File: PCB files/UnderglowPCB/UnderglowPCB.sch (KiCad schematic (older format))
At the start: 67 parts, among them J1 USB_B_Micro, J12 DB9_Male, J4 Conn_01x07, J5 Conn_01x05, J7 Screw_Terminal_01x03, J8 Screw_Terminal_01x03, Q1 S8050, Q2 S8050, SW1 SW_Push, U1 CP2102N-A01-GQFN28, U2 TPS62133, U3 74HC14, U4 74HC14, U5 LD56100DPU33R, U6 ESP32-WROOM-32D, U7 SN65HVD230, U8 USBLC6-2SC6

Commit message: Version 1.0.0 of PCB is almost done. Need tooling holes and holds for DB9 mount.
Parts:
- removed SW1: SW_Push, Button_Switch_SMD:SW_SPST_TL3305A, symbol Switch:SW_Push
- J1: footprint Connector_USB:USB_Micro-B_Molex-105017-0001 -> Connector_USB:USB_Micro-AB_Molex_47590-0001
- J10, J11, J3, J6, J9: renamed from J?; footprint TerminalBlock_Phoenix:TerminalBlock_Phoenix_MKDS-1,5-3-5.08_1x03_P5.08mm_Horizontal -> Connector_PinHeader_2.54mm:PinHeader_1x03_P2.54mm_Vertical
- J2: renamed from J?; footprint TerminalBlock_Phoenix:TerminalBlock_Phoenix_MKDS-1,5-3-5.08_1x03_P5.08mm_Horizontal -> Connector_PinSocket_2.54mm:PinSocket_1x03_P2.54mm_Vertical
- J7, J8: footprint TerminalBlock_Phoenix:TerminalBlock_Phoenix_MKDS-1,5-3-5.08_1x03_P5.08mm_Horizontal -> Connector_PinHeader_2.54mm:PinHeader_1x03_P2.54mm_Vertical
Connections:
- net labels added: CAR_12V
- wire segments 167 -> 162
- no-connect marks 33 -> 31
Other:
- moved on the sheet: D4

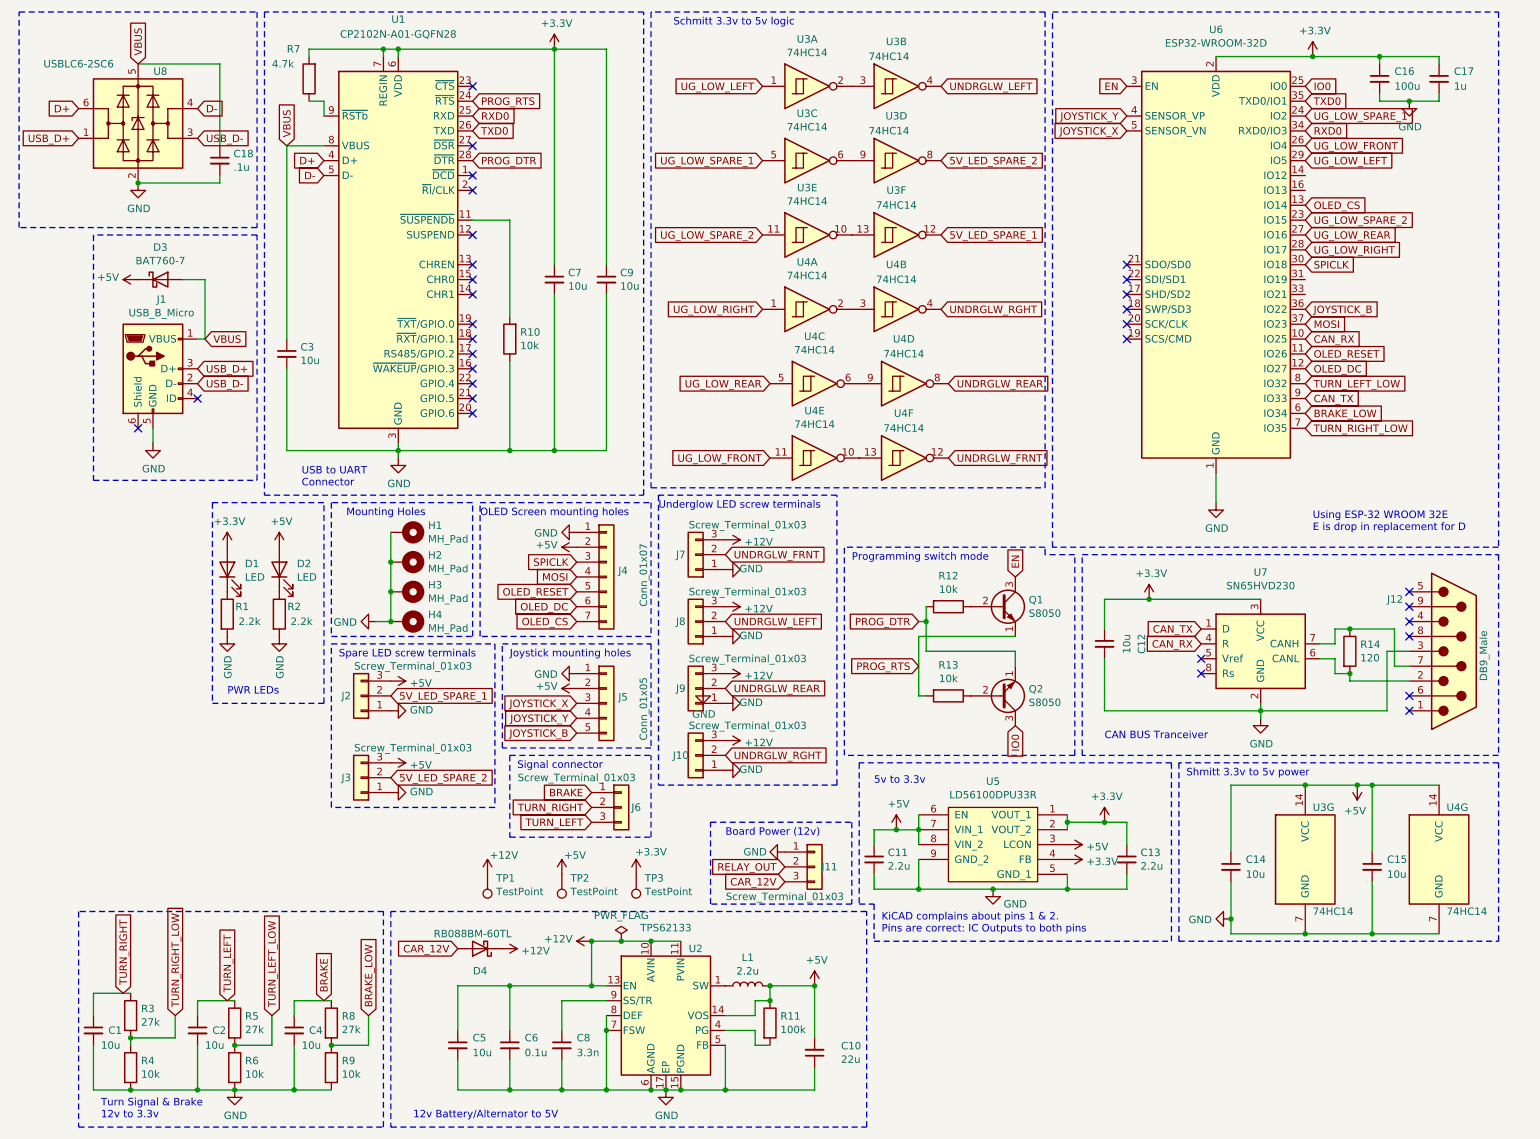
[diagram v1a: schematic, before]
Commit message: Posted to reddit, changes include TVS Zener diodes and new power solution. That's a lot bigger.
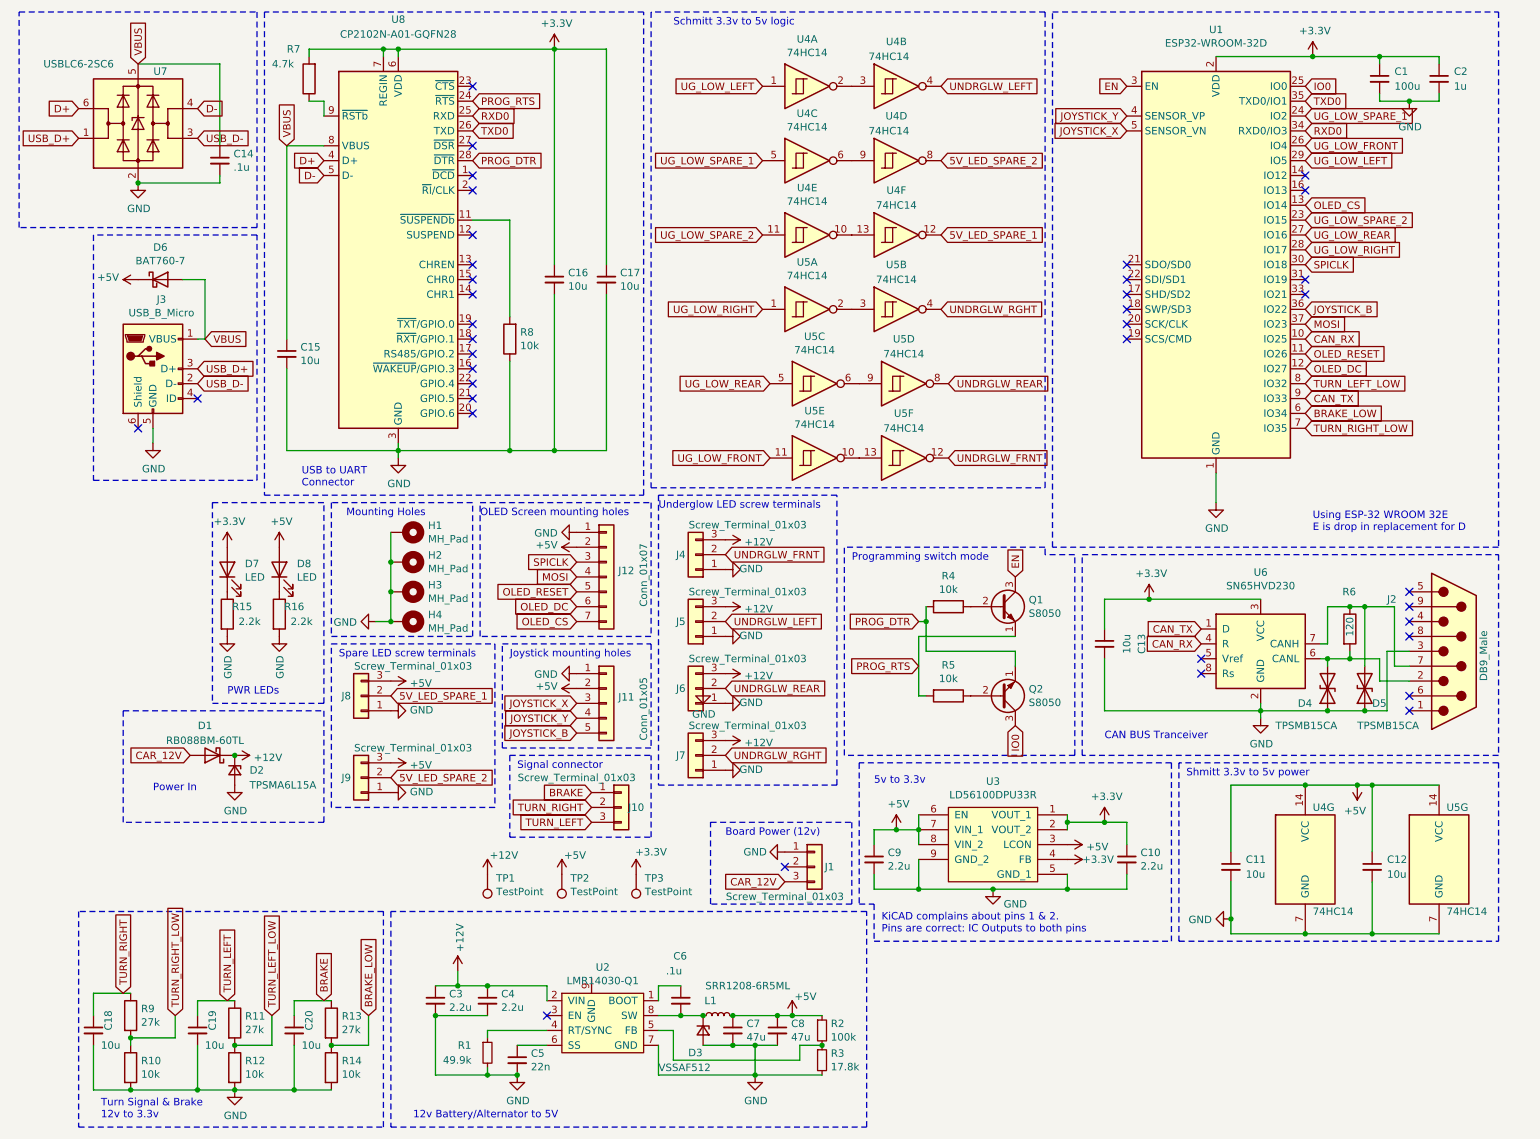
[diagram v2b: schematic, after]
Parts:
- removed C10: 22u, Capacitor_SMD:C_0805_2012Metric, symbol Device:C_Small
- removed L1: 2.2u, Inductor_SMD:L_Coilcraft_XxL4020, symbol Device:L
- removed R11: 100k, Resistor_SMD:R_0603_1608Metric, symbol Device:R
- removed U2: TPS62133, Package_DFN_QFN:VQFN-16-1EP_3x3mm_P0.5mm_EP1.68x1.68mm_ThermalVias, symbol Regulator_Switching:TPS62133
- added C3, C4: 2.2u, Capacitor_SMD:C_0603_1608Metric, symbol Device:C_Small
- added C7: 47u, Capacitor_SMD:C_1210_3225Metric, symbol Device:C_Small
- added D2: TPSMA6L15A, UnderglowPCB:TPSMA6L15A, symbol Device:D_Zener_Small
- added D3: VSSAF512, UnderglowPCB:TPSMA6L15A, symbol Device:D_Zener_Small
- added D4, D5: TPSMB15CA, UnderglowPCB:TPSMB15CA, symbol Device:D_TVS
- added L1: SRR1208-6R5ML, UnderglowPCB:SRR1208, symbol Device:L_Small
- added R1: 49.9k, Resistor_SMD:R_0603_1608Metric, symbol Device:R_Small
- added R2: 100k, Resistor_SMD:R_0603_1608Metric, symbol Device:R_Small
- added R3: 17.8k, Resistor_SMD:R_0603_1608Metric, symbol Device:R_Small
- added U2: LMR14030-Q1, Package_SO:Texas_HSOP-8-1EP_3.9x4.9mm_P1.27mm_ThermalVias, symbol ExternalPartsLib:LMR14030-Q1
- C14: renamed from C18; footprint Capacitor_SMD:C_0402_1005Metric -> Capacitor_SMD:C_0603_1608Metric
- C5: value 10u -> 22n; footprint Capacitor_SMD:C_1210_3225Metric -> Capacitor_SMD:C_0603_1608Metric
- C6: value 0.1u -> .1u
- C8: value 3.3n -> 47u; footprint Capacitor_SMD:C_0603_1608Metric -> Capacitor_SMD:C_1210_3225Metric
- renumbered C16 to C1, C13 to C10, C14 to C11, C15 to C12, C12 to C13, C3 to C15, C7 to C16, C9 to C17, C1 to C18, C2 to C19, C17 to C2, C4 to C20, C11 to C9, D4 to D1, D3 to D6, D1 to D7, D2 to D8, J11 to J1, J6 to J10, J5 to J11, J4 to J12, J12 to J2, J1 to J3, J7 to J4, J8 to J5, J9 to J6, J10 to J7, J2 to J8, J3 to J9, R4 to R10, R5 to R11, R6 to R12, R8 to R13, R9 to R14, R1 to R15, R2 to R16, R12 to R4, R13 to R5, R14 to R6, R10 to R8, R3 to R9, U6 to U1, U5 to U3, U3 to U4, U4 to U5, U7 to U6, U8 to U7, U1 to U8
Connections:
- net +12V: now also C3.1, C4.1, D2.1 (K), U2.2 (VIN); no longer C5.1, C6.1
- net +5V: now also C8.1, C7.1, L1.2, R2.1
- net GND: now also C3.2, C4.2, C7.2, D2.2 (A), D3.2 (A), D4.1 (A1), D5.1 (A1), R1.2, R3.2, U2.7 (GND); no longer C6.2
- net at J2.2, R6.2, U6.6 (CANL): now also D4.2 (A2)
- net at J2.7, R6.1, U6.7 (CANH): now also D5.2 (A2)
- net RELAY_OUT: no longer names the net of J1.2 (Pin_2)
- new net: C6.1, U2.1 (BOOT)
- new net: R1.1, U2.4 (RT/SYNC)
- new net: R2.2, R3.1, U2.5 (FB)
- new net: C5.1, U2.6 (SS)
- new net: C6.2, D3.1 (K), L1.1, U2.8 (SW)
- no-connect marks 31 -> 37
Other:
- note added: "Power In"
- moved on the sheet: D1, R6

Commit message: Lastest draft of device
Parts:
- removed TP1, TP2, TP3: TestPoint, TestPoint:TestPoint_Plated_Hole_D2.0mm, symbol Connector:TestPoint
- removed U3: LD56100DPU33R, UnderglowPCB:LD56100DPU33R, symbol ExternalPartsLib:LD56100DPU33R
- added F1: 3413.0330.22, Fuse:Fuse_1206_3216Metric, symbol Device:Fuse_Small
- added U3: NCP1117-3.3_SOT223, Package_TO_SOT_SMD:SOT-223-3_TabPin2, symbol Regulator_Linear:NCP1117-3.3_SOT223
- C10, C9: value 2.2u -> 10u
- J2: footprint Connector_Dsub:DSUB-9_Male_Horizontal_P2.77x2.84mm_EdgePinOffset9.40mm -> UnderglowPCB:DB9
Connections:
- net +12V: no longer D2.1 (K)
- net +3V3: now also J11.2 (Pin_2), U3.2 (VO)
- net +5V: now also U3.3 (VI); no longer J11.2 (Pin_2)
- net 5V_LED_SPARE_1: now also U4.10; no longer U4.12
- net 5V_LED_SPARE_2: now also U4.8; no longer U4.8
- net CAR_12V: now also D2.1 (K), F1.1; no longer D1.2 (A)
- net GND: now also U2.9 (GND), U3.1 (GND)
- net UG_LOW_FRONT: now also U5.1; no longer U5.11
- net UG_LOW_LEFT: now also U5.3; no longer U4.1
- net UG_LOW_REAR: now also U5.5; no longer U5.5
- net UG_LOW_RIGHT: now also U4.1; no longer U5.1
- net UG_LOW_SPARE_1: now also U4.5; no longer U4.5
- net UG_LOW_SPARE_2: now also U4.3; no longer U4.11
- net UNDRGLW_FRNT: now also U5.12; no longer U5.12
- net UNDRGLW_LEFT: now also U5.10; no longer U4.4
- net UNDRGLW_REAR: now also U5.8; no longer U5.8
- net UNDRGLW_RGHT: now also U4.12; no longer U5.4
- net at U4.2: now also U4.13; no longer U4.3
- net at U5.2: now also U5.13; no longer U5.3
- new net: D1.2 (A), F1.2
- new net: U4.11, U4.4
- new net: U4.6, U4.9
- new net: U5.11, U5.4
- new net: U5.6, U5.9
- no-connect marks 37 -> 40
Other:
- note removed: "KiCAD complains about pins 1 & 2.\nPins are correct: IC Outputs to both pins"
- moved on the sheet: D1, D2

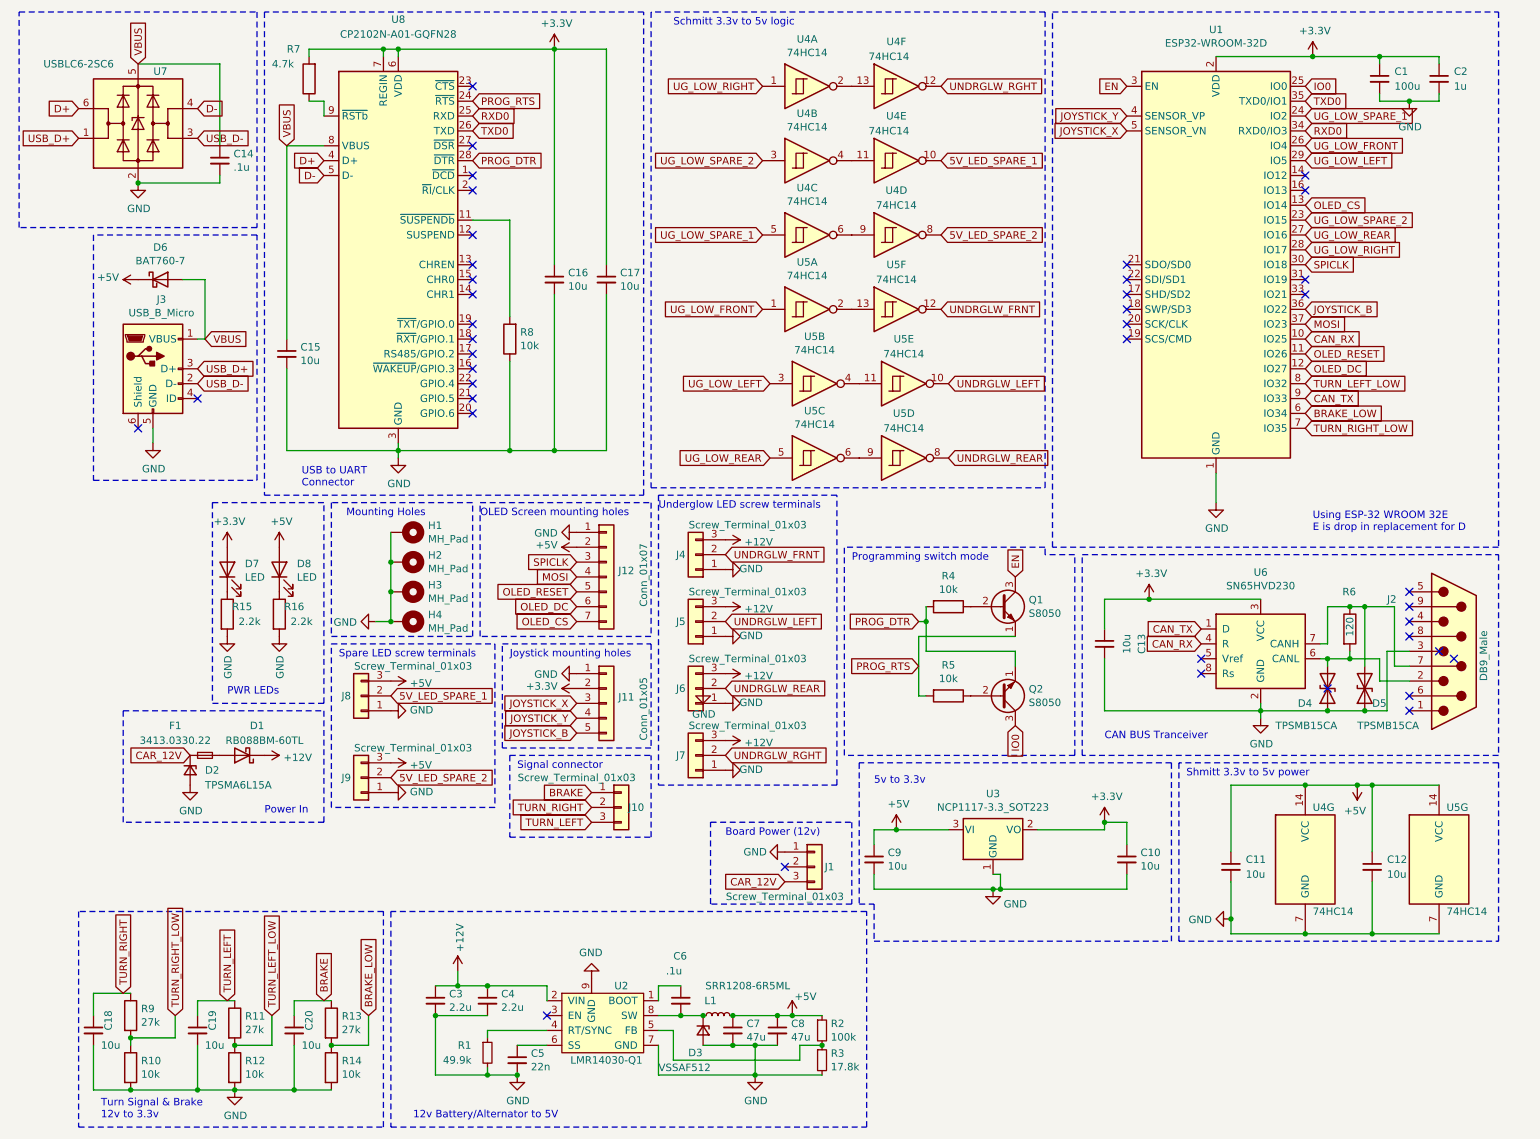
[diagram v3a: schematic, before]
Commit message: PCB 1.2 finished. Needs some silkscreen work.
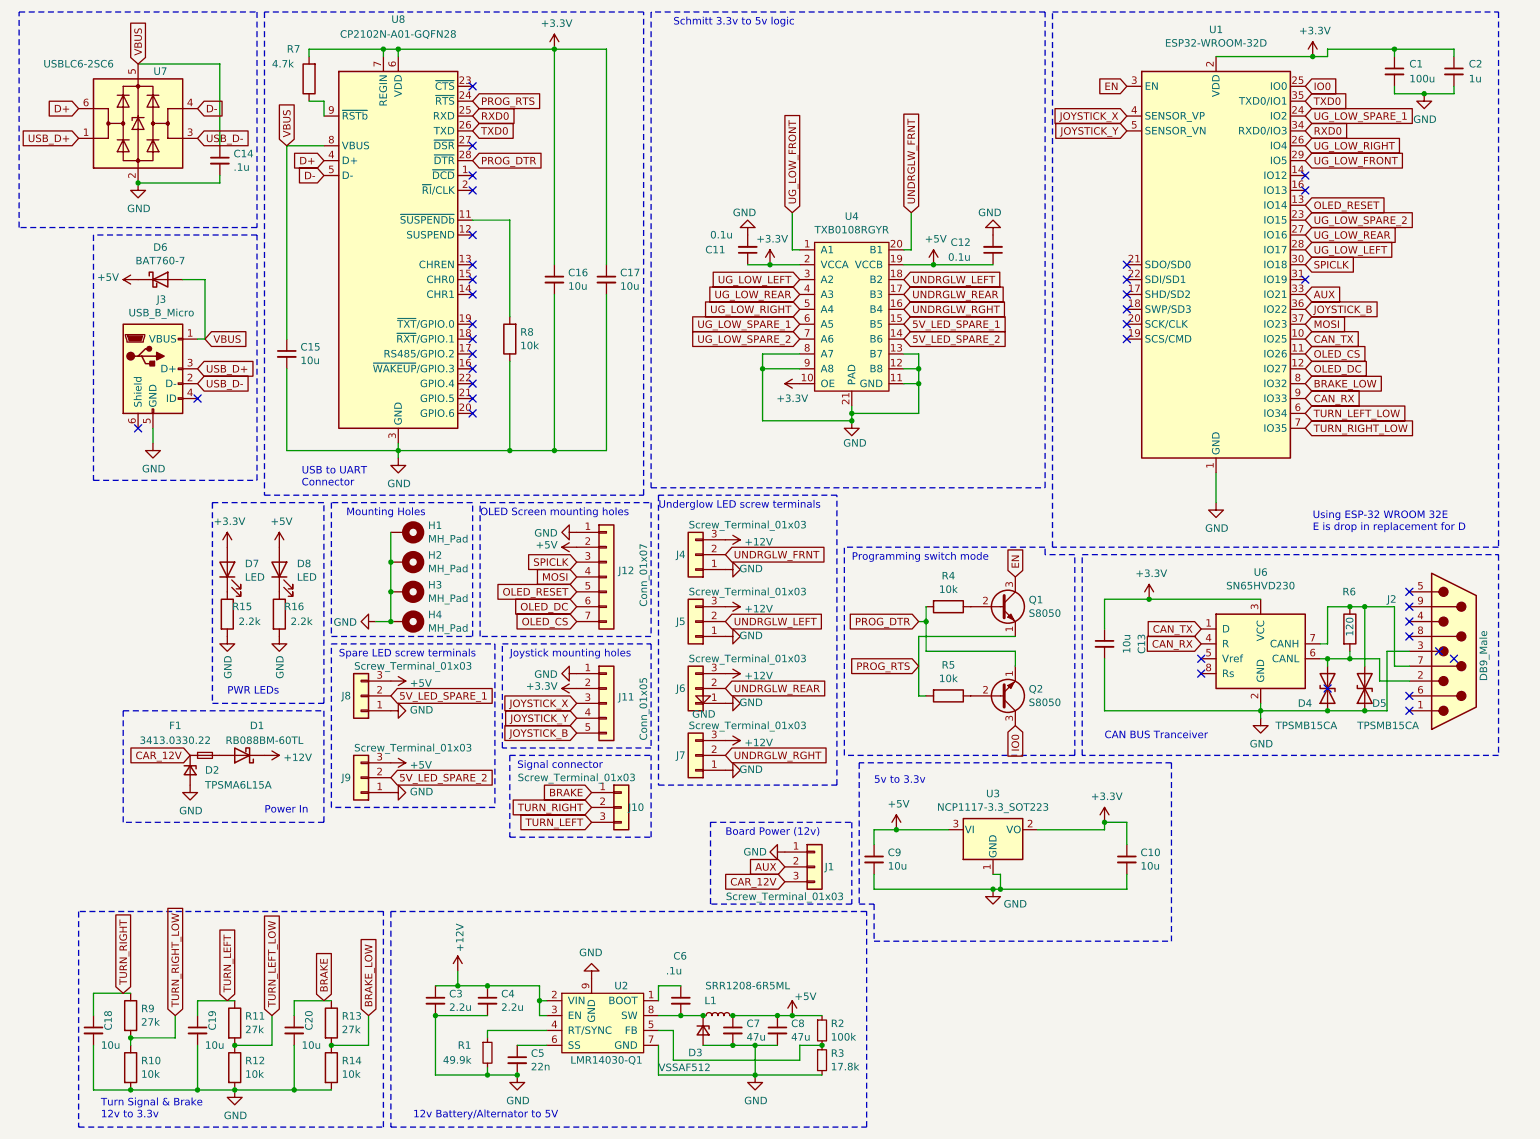
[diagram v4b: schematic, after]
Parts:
- removed U4, U5: 74HC14, Package_DIP:DIP-14_W7.62mm_SMDSocket_SmallPads, symbol 74xx:74HC14
- added U4: TXB0108RGYR, UnderglowPCB:VQFN-20, symbol ExternalPartsLib:TXB0108RGYR
- C11, C12: value 10u -> 0.1u
- J11: footprint Connector_PinHeader_2.54mm:PinHeader_1x05_P2.54mm_Vertical -> UnderglowPCB:Joystick_Header
- J12: footprint Connector_PinHeader_2.54mm:PinHeader_1x07_P2.54mm_Vertical -> UnderglowPCB:SSD1306_Footprint
- J8: footprint Connector_PinSocket_2.54mm:PinSocket_1x03_P2.54mm_Vertical -> Connector_PinHeader_2.54mm:PinHeader_1x03_P2.54mm_Vertical
- U6: footprint Package_SO:SOIC-8_3.9x4.9mm_P1.27mm -> UnderglowPCB:Texas_HSOP-8-1EP_3.9x4.9mm_P1.27mm_ThermalVias
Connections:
- net +12V: now also U2.3 (EN)
- net +3V3: now also C11.1, U4.10 (OE), U4.2 (VCCA)
- net +5V: now also U4.19 (VCCB); no longer C11.1
- net 5V_LED_SPARE_1: now also U4.15 (B5)
- net 5V_LED_SPARE_2: now also U4.14 (B6)
- net BRAKE_LOW: now also U1.8 (IO32); no longer U1.6 (IO34)
- net CAN_RX: now also U1.9 (IO33); no longer U1.10 (IO25)
- net CAN_TX: now also U1.10 (IO25); no longer U1.9 (IO33)
- net GND: now also U4.11 (GND), U4.12 (B8), U4.13 (B7), U4.21 (PAD), U4.8 (A7), U4.9 (A8)
- net JOYSTICK_X: now also U1.4 (SENSOR_VP); no longer U1.5 (SENSOR_VN)
- net JOYSTICK_Y: now also U1.5 (SENSOR_VN); no longer U1.4 (SENSOR_VP)
- net OLED_CS: now also U1.11 (IO26); no longer U1.13 (IO14)
- net OLED_RESET: now also U1.13 (IO14); no longer U1.11 (IO26)
- net TURN_LEFT_LOW: now also U1.6 (IO34); no longer U1.8 (IO32)
- net UG_LOW_FRONT: now also U1.29 (IO5), U4.1 (A1); no longer U1.26 (IO4)
- net UG_LOW_LEFT: now also U1.28 (IO17), U4.3 (A2); no longer U1.29 (IO5)
- net UG_LOW_REAR: now also U4.4 (A3)
- net UG_LOW_RIGHT: now also U1.26 (IO4), U4.5 (A4); no longer U1.28 (IO17)
- net UG_LOW_SPARE_1: now also U4.6 (A5)
- net UG_LOW_SPARE_2: now also U4.7 (A6)
- net UNDRGLW_FRNT: now also U4.20 (B1)
- net UNDRGLW_LEFT: now also U4.18 (B2)
- net UNDRGLW_REAR: now also U4.17 (B3)
- net UNDRGLW_RGHT: now also U4.16 (B4)
- net AUX: now reaches U1.33 (IO21)
- net AUX: now also J1.2 (Pin_2)
- no-connect marks 40 -> 37
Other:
- note removed: "Shmitt 3.3v to 5v power"
- moved on the sheet: C1, C11, C12, C2
